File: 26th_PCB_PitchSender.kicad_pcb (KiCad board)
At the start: 2 copper layers, 120.2 x 28.5 mm, 22 parts, among them J1 Amp, J2 Conn_01x04_Pin, J3 microSD, J4 BNO055, J5 BNO055, J6 BMP390

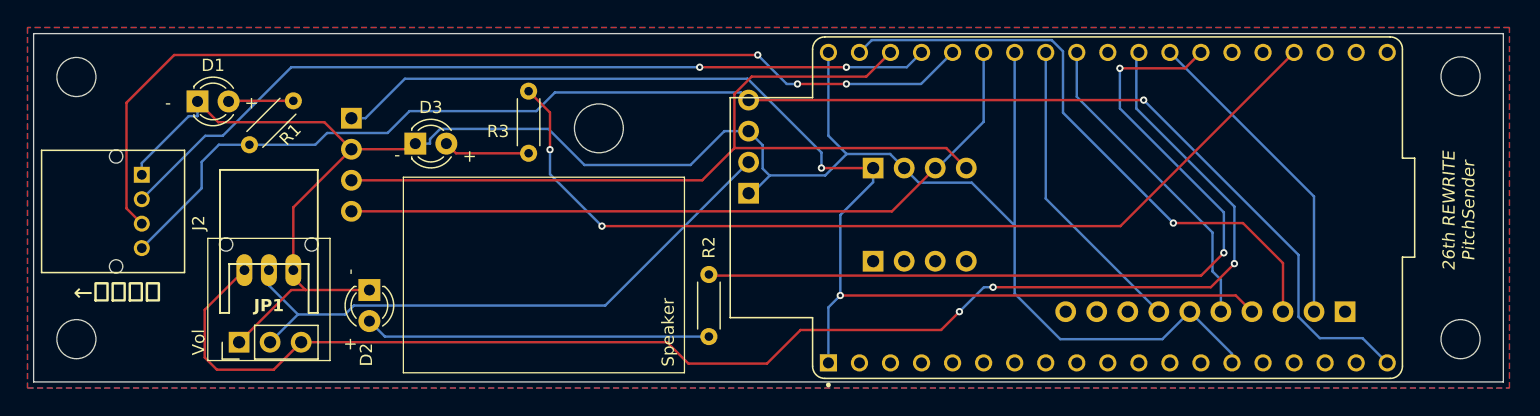
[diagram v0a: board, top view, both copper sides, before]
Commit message: コネクタ向き修正
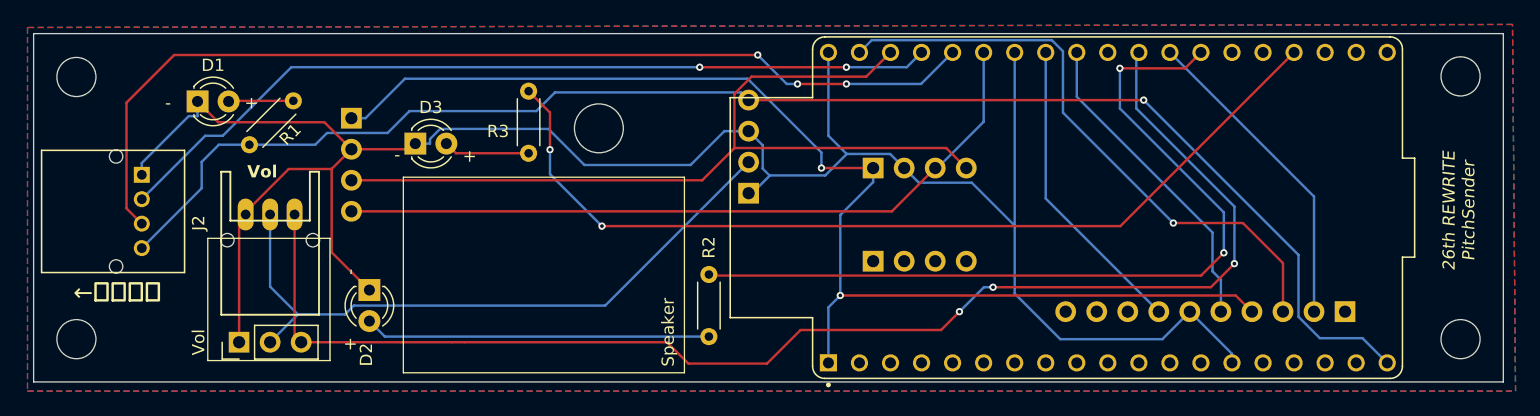
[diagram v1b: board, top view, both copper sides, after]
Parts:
- JP1: value S03B-PASK-2 -> Vol
- moved JP1 4.55 mm to (120.8, 91.3), turned to 180 degrees
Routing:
- net /SPK: track 119.9 -> 111.8 mm
- net GND: track 167.1 -> 175.1 mm
- net Net-(J1-Pin_2): track 49.9 -> 54.4 mm

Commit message: UART/LEDピン変更
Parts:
- JP1: value Vol -> S03B-PASK-2
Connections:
- R3 pad 1: Net-(U1-IO15) -> Net-(U1-IO25)
- U1 pad J2_7: unconnected-(U1-IO32-PadJ2_7) -> /BicoTX-psdRX
- U1 pad J2_8: unconnected-(U1-IO33-PadJ2_8) -> /BicoRX-psdTX
- U1 pad J2_9: unconnected-(U1-IO25-PadJ2_9) -> Net-(U1-IO25)
- U1 pad J3_16: Net-(U1-IO15) -> unconnected-(U1-IO15-PadJ3_16)
- U1 pad J3_4: /BicoRX-psdTX -> unconnected-(U1-TXD0-PadJ3_4)
- U1 pad J3_5: /BicoTX-psdRX -> unconnected-(U1-RXD0-PadJ3_5)
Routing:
- net Net-(U1-IO15): track 76.0 -> 0.00 mm, vias 2 -> 0
- net Net-(U1-IO25): track 0.00 -> 59.0 mm, vias 0 -> 2
- net /BicoRX-psdTX: track 68.8 -> 83.8 mm, vias 2 -> 5
- net /BicoTX-psdRX: track 81.7 -> 86.7 mm, vias 3 -> 2
